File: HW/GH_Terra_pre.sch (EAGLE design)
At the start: 37 parts, among them Q1 IRLML6402, Q2 IRLML6244, Q4 IRLML6402, Q5 IRLML6244, U1 STM8L152C6T6, U7 MA02-1

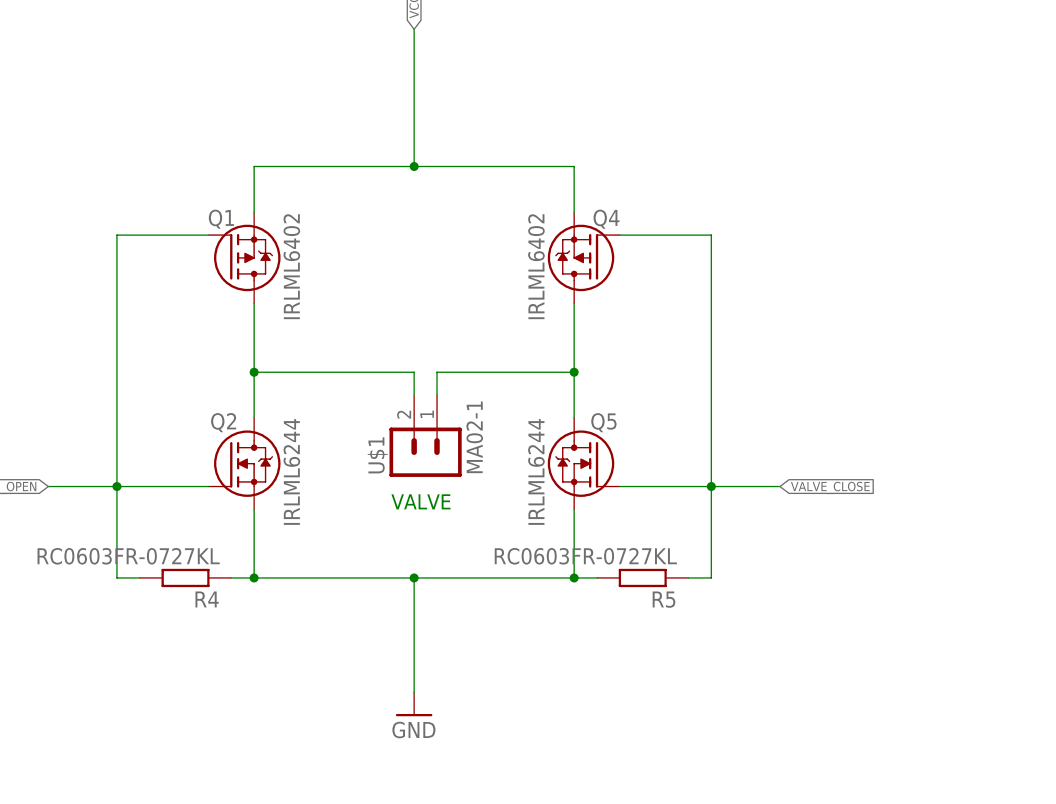
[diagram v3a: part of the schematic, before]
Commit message: Введено: Защитный интервал между поливами. В сервисное меню добавлена настройка защитного интервала
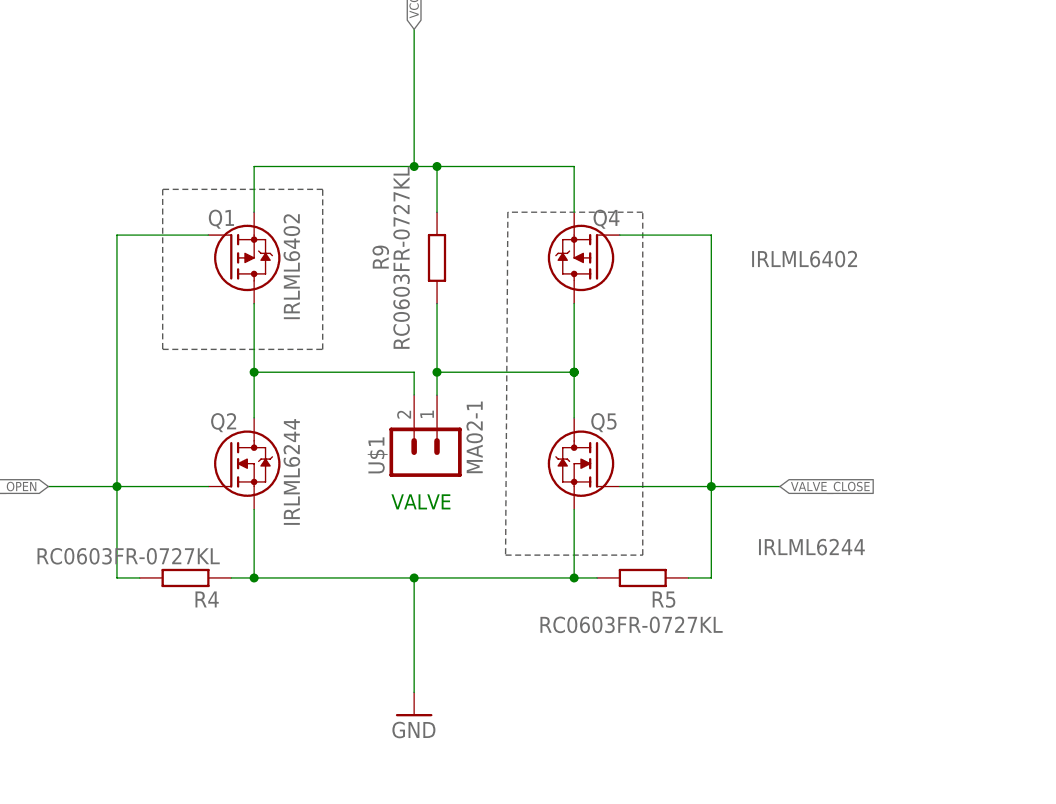
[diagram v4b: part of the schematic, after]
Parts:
- added R9: RC0603FR-0727KL, rcl:R-EU_R0603
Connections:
- net N$3: now also R9.2
- net VCC: now also R9.1
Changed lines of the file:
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@@
 <part name="U7" library="con-lstb" deviceset="MA02-1" device=""/>
 <part name="GND10" library="supply1" deviceset="GND" device=""/>
+<part name="R9" library="rcl" deviceset="R-EU_" device="R0603" value="RC0603FR-0727KL"/>
 </parts>
 <sheets>
@@
 <frame x1="-198.12" y1="-175.26" x2="302.26" y2="88.9" columns="8" rows="5" layer="97"/>
 <text x="251.46" y="-134.62" size="1.778" layer="91">SENSOR_OF_POSITION</text>
+<wire x1="-25.4" y1="-99.06" x2="-7.62" y2="-99.06" width="0.1524" layer="97" style="shortdash"/>
+<wire x1="-7.62" y1="-99.06" x2="-7.62" y2="-81.28" width="0.1524" layer="97" style="shortdash"/>
+<wire x1="-7.62" y1="-81.28" x2="-25.4" y2="-81.28" width="0.1524" layer="97" style="shortdash"/>
+<wire x1="-25.4" y1="-81.28" x2="-25.4" y2="-99.06" width="0.1524" layer="97" style="shortdash"/>
+<wire x1="12.7" y1="-121.92" x2="27.94" y2="-121.92" width="0.1524" layer="97" style="shortdash"/>
+<wire x1="27.94" y1="-121.92" x2="27.94" y2="-83.82" width="0.1524" layer="97" style="shortdash"/>
+<wire x1="27.94" y1="-83.82" x2="12.954" y2="-83.82" width="0.1524" layer="97" style="shortdash"/>
+<wire x1="12.954" y1="-83.82" x2="12.7" y2="-121.92" width="0.1524" layer="97" style="shortdash"/>
 </plain>
 <instances>
@@
 </instance>
 <instance part="Q4" gate="G$1" x="22.86" y="-88.9" smashed="yes" rot="MR0">
-<attribute name="VALUE" x="17.018" y="-83.82" size="1.778" layer="96" rot="MR270"/>
+<attribute name="VALUE" x="39.878" y="-88.138" size="1.778" layer="96" rot="MR180"/>
 <attribute name="NAME" x="22.352" y="-85.344" size="1.778" layer="95"/>
 </instance>
 <instance part="Q5" gate="G$1" x="22.86" y="-111.76" smashed="yes" rot="MR0">
-<attribute name="VALUE" x="17.018" y="-106.68" size="1.778" layer="96" rot="MR270"/>
+<attribute name="VALUE" x="40.64" y="-120.142" size="1.778" layer="96" rot="MR180"/>
 <attribute name="NAME" x="22.098" y="-107.95" size="1.778" layer="95"/>
 </instance>
@@
 <instance part="R5" gate="G$1" x="27.94" y="-124.46" smashed="yes" rot="R180">
 <attribute name="NAME" x="31.75" y="-125.9586" size="1.778" layer="95" rot="R180"/>
-<attribute name="VALUE" x="31.75" y="-121.158" size="1.778" layer="96" rot="R180"/>
+<attribute name="VALUE" x="36.83" y="-128.778" size="1.778" layer="96" rot="R180"/>
 </instance>
 <instance part="U$1" gate="G$1" x="2.54" y="-111.76" rot="R90"/>
@@
 <instance part="GND10" gate="1" x="241.3" y="-147.32" smashed="yes">
 <attribute name="VALUE" x="238.76" y="-149.86" size="1.778" layer="96"/>
+</instance>
+<instance part="R9" gate="G$1" x="5.08" y="-88.9" smashed="yes" rot="R270">
+<attribute name="NAME" x="-2.0574" y="-87.376" size="1.778" layer="95" rot="R270"/>
+<attribute name="VALUE" x="0.254" y="-78.74" size="1.778" layer="96" rot="R270"/>
 </instance>
 </instances>
@@
 <wire x1="-15.24" y1="-78.74" x2="2.54" y2="-78.74" width="0.1524" layer="91"/>
 <pinref part="Q4" gate="G$1" pin="S"/>
-<wire x1="2.54" y1="-78.74" x2="20.32" y2="-78.74" width="0.1524" layer="91"/>
+<wire x1="2.54" y1="-78.74" x2="5.08" y2="-78.74" width="0.1524" layer="91"/>
+<junction x="2.54" y="-78.74"/>
 <wire x1="20.32" y1="-78.74" x2="20.32" y2="-83.82" width="0.1524" layer="91"/>
-<junction x="2.54" y="-78.74"/>
 <wire x1="2.54" y1="-63.5" x2="2.54" y2="-78.74" width="0.1524" layer="91"/>
+<pinref part="R9" gate="G$1" pin="1"/>
+<wire x1="5.08" y1="-83.82" x2="5.08" y2="-78.74" width="0.1524" layer="91"/>
+<wire x1="5.08" y1="-78.74" x2="20.32" y2="-78.74" width="0.1524" layer="91"/>
+<junction x="5.08" y="-78.74"/>
 </segment>
 <segment>
@@
 <wire x1="5.08" y1="-104.14" x2="5.08" y2="-101.6" width="0.1524" layer="91"/>
 <junction x="20.32" y="-101.6"/>
+<pinref part="R9" gate="G$1" pin="2"/>
+<wire x1="5.08" y1="-93.98" x2="5.08" y2="-101.6" width="0.1524" layer="91"/>
 <wire x1="5.08" y1="-101.6" x2="20.32" y2="-101.6" width="0.1524" layer="91"/>
-</segment>
-</net>
+<junction x="20.32" y="-101.6"/>
+<junction x="5.08" y="-101.6"/>
+</segment>
+</net>

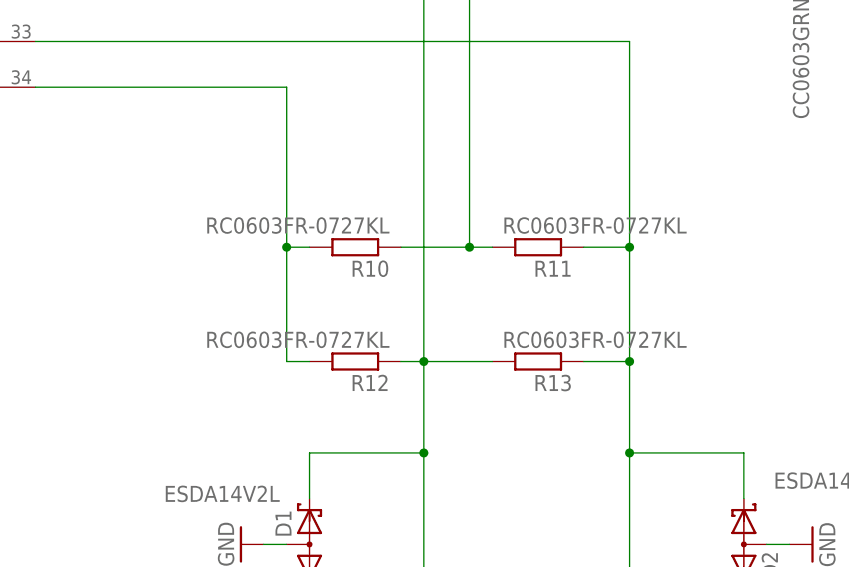
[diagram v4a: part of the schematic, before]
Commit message: Версия для односторонней платой. Первая редакция. Перенастроены порты и проверены все основные функции
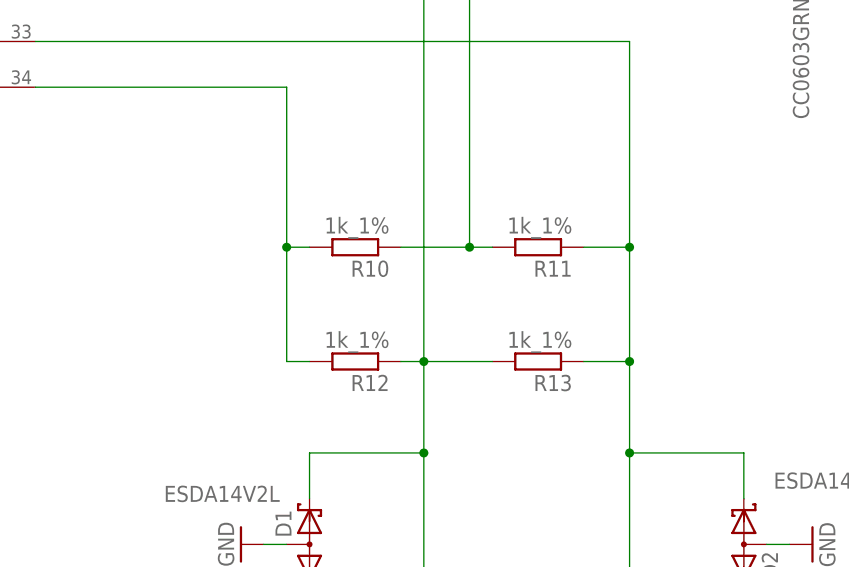
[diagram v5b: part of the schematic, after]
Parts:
- R10, R11, R12, R13: value RC0603FR-0727KL -> 1k_1%
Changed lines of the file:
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@@
 <parts>
 <part name="U1" library="st-microelectronics" deviceset="STM8L152C6" device="" value="STM8L152C6T6"/>
-<part name="R10" library="rcl" deviceset="R-EU_" device="R0603" value="RC0603FR-0727KL"/>
-<part name="R11" library="rcl" deviceset="R-EU_" device="R0603" value="RC0603FR-0727KL"/>
-<part name="R12" library="rcl" deviceset="R-EU_" device="R0603" value="RC0603FR-0727KL"/>
-<part name="R13" library="rcl" deviceset="R-EU_" device="R0603" value="RC0603FR-0727KL"/>
+<part name="R10" library="rcl" deviceset="R-EU_" device="R0603" value="1k_1%"/>
+<part name="R11" library="rcl" deviceset="R-EU_" device="R0603" value="1k_1%"/>
+<part name="R12" library="rcl" deviceset="R-EU_" device="R0603" value="1k_1%"/>
+<part name="R13" library="rcl" deviceset="R-EU_" device="R0603" value="1k_1%"/>
 <part name="U$2" library="rubber_key" deviceset="RK_4X3" device=""/>
 <part name="U$3" library="rubber_key" deviceset="RK_4X3" device=""/>
@@
 <instance part="R11" gate="G$1" x="147.32" y="-68.58" smashed="yes" rot="R180">
 <attribute name="NAME" x="151.13" y="-70.0786" size="1.778" layer="95" rot="R180"/>
-<attribute name="VALUE" x="163.83" y="-65.278" size="1.778" layer="96" rot="R180"/>
+<attribute name="VALUE" x="151.13" y="-65.278" size="1.778" layer="96" rot="R180"/>
 </instance>
 <instance part="R12" gate="G$1" x="127" y="-81.28" smashed="yes" rot="R180">
@@
 <instance part="R13" gate="G$1" x="147.32" y="-81.28" smashed="yes" rot="R180">
 <attribute name="NAME" x="151.13" y="-82.7786" size="1.778" layer="95" rot="R180"/>
-<attribute name="VALUE" x="163.83" y="-77.978" size="1.778" layer="96" rot="R180"/>
+<attribute name="VALUE" x="151.13" y="-77.978" size="1.778" layer="96" rot="R180"/>
 </instance>
 <instance part="U$2" gate="G$1" x="223.52" y="15.24"/>
